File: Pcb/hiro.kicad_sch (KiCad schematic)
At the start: 0 parts

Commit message: schematic parts
added a really nice microsd card slot, an esp32-s3, and an audio jack.
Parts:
- added J1: Micro_SD_Card_Det_Hirose_DM3AT, symbol Connector:Micro_SD_Card_Det_Hirose_DM3AT
- added J2: AudioJack3, Connector_Audio:Jack_3.5mm_CUI_SJ-3523-SMT_Horizontal, symbol Connector_Audio:AudioJack3
- added U1: XIAO-ESP32-S3-Plus-SMD, Seeed_Studio_XIAO_Series:XIAO-ESP32-S3-Plus-SMD, symbol Seeed_Studio_XIAO_Series:XIAO-ESP32-S3 Plus-SMD
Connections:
- new net +3.3V: J1.4 (VDD)
- new net CLK: J1.5 (CLK), U1.23 (GPIO13_DVP_PCLK_SPI_SCK1)
- new net CMD: J1.3 (CMD), U1.21 (GPIO11_DVP_Y8_SPI_MOSI1)
- new net DAT0: J1.7 (DAT0), U1.22 (GPIO12_DVP_Y7_SPI_MISO1)
- new net DAT3: J1.2 (DAT3/CD)
- new net GND: J1.6 (VSS)
- no-connect marks 0 -> 2

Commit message: sooooooooooooooo much work
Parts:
- added C1, C4, C5, C6: 10 µF, Capacitor_SMD:C_01005_0402Metric_Pad0.57x0.30mm_HandSolder, symbol Device:C
- added C2, C3: 100nF, Capacitor_SMD:C_01005_0402Metric_Pad0.57x0.30mm_HandSolder, symbol Device:C
- added J3: Conn_01x08, symbol Connector_Generic:Conn_01x08
- added SW1, SW2: SW_Push, symbol Switch:SW_Push
- added U2: PCM5102A, Package_SO:TSSOP-20_4.4x6.5mm_P0.65mm, symbol Audio:PCM5102A
- J1: footprint (none) -> Connector_Card:microSD_HC_Hirose_DM3AT-SF-PEJM5
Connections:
- net +3.3V: now also U1.12 (3V3), C4.1, J3.1 (Pin_1), U2.17 (XSMT); no longer J1.4 (VDD)
- net CLK: now also U1.9 (GPIO7_A8_D8_SCK), J3.4 (Pin_4); no longer J1.5 (CLK), U1.23 (GPIO13_DVP_PCLK_SPI_SCK1)
- net GND: now also J2.S, U1.13 (GND), C2.1, C3.1, C4.2, C5.2, C6.2, J3.2 (Pin_2), U2.1 (CPVDD), U2.10 (DEMP), U2.11 (FLT), U2.16 (FMT), U2.19 (DGND), U2.3 (CPGND), U2.9 (AGND); no longer J1.6 (VSS)
- net at J2.R: now also U2.7 (OUTR)
- net at J2.T: now also U2.6 (OUTL)
- net CS: now reaches U1.10 (GPIO8_A9_D9_MISO)
- net CS: now also J3.5 (Pin_5)
- net DIN: now reaches U1.11 (GPIO9_A10_D10_MOSI)
- net DIN: now also J3.3 (Pin_3)
- net DC: now reaches U1.8 (GPIO44_D7_RX)
- net DC: now also J3.6 (Pin_6)
- net CMD: no longer names the net of J1.3 (CMD)
- net CMD: no longer U1.21 (GPIO11_DVP_Y8_SPI_MOSI1)
- net DAT0: no longer names the net of J1.7 (DAT0)
- net DAT0: no longer U1.22 (GPIO12_DVP_Y7_SPI_MISO1)
- net DAT3: no longer names the net of J1.2 (DAT3/CD)
- new net: C5.1, U2.18 (LDOO)
- new net: C1.1, U2.2 (CAPP)
- new net: C3.2, U2.20 (DVDD)
- new net: C1.2, U2.4 (CAPM)
- new net: C6.1, U2.5 (VNEG)
- new net: C2.2, U2.8 (AVDD)
- new net BCK: U2.13 (BCK)
- new net BL: J3.8 (Pin_8), U1.22 (GPIO12_DVP_Y7_SPI_MISO1)
- new net DIN2: U2.14 (DIN)
- new net LCK: U2.15 (LRCK)
- new net RST: J3.7 (Pin_7), U1.21 (GPIO11_DVP_Y8_SPI_MOSI1)
- no-connect marks 2 -> 1
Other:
- moved on the sheet: J2

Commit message: THE OUTLINE WORKS YAYYY
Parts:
- C1, C2, C3, C4, C5, C6: footprint Capacitor_SMD:C_01005_0402Metric_Pad0.57x0.30mm_HandSolder -> Capacitor_SMD:C_0603_1608Metric_Pad1.08x0.95mm_HandSolder
- J3: footprint (none) -> Connector_PinHeader_2.54mm:PinHeader_1x08_P2.54mm_Vertical
- U1: footprint Seeed_Studio_XIAO_Series:XIAO-ESP32-S3-Plus-SMD -> New_XIAO_Series_Footprints:XIAO-ESP32-S3-Plus-SMD
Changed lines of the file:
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@@
 			)
 		)
-		(property "Footprint" "Capacitor_SMD:C_01005_0402Metric_Pad0.57x0.30mm_HandSolder"
+		(property "Footprint" "Capacitor_SMD:C_0603_1608Metric_Pad1.08x0.95mm_HandSolder"
 			(at 159.7152 59.69 0)
 			(hide yes)
@@
 			)
 		)
-		(property "Footprint" "Capacitor_SMD:C_01005_0402Metric_Pad0.57x0.30mm_HandSolder"
+		(property "Footprint" "Capacitor_SMD:C_0603_1608Metric_Pad1.08x0.95mm_HandSolder"
 			(at 179.07 86.6648 0)
 			(hide yes)
@@
 			)
 		)
-		(property "Footprint" "Capacitor_SMD:C_01005_0402Metric_Pad0.57x0.30mm_HandSolder"
+		(property "Footprint" "Capacitor_SMD:C_0603_1608Metric_Pad1.08x0.95mm_HandSolder"
 			(at 162.2552 59.69 0)
 			(hide yes)
@@
 			)
 		)
-		(property "Footprint" "Capacitor_SMD:C_01005_0402Metric_Pad0.57x0.30mm_HandSolder"
+		(property "Footprint" "Capacitor_SMD:C_0603_1608Metric_Pad1.08x0.95mm_HandSolder"
 			(at 135.5852 46.99 0)
 			(hide yes)
@@
 			)
 		)
-		(property "Footprint" "Capacitor_SMD:C_01005_0402Metric_Pad0.57x0.30mm_HandSolder"
+		(property "Footprint" "Capacitor_SMD:C_0603_1608Metric_Pad1.08x0.95mm_HandSolder"
 			(at 172.4152 80.01 0)
 			(hide yes)
@@
 			)
 		)
-		(property "Footprint" "Capacitor_SMD:C_01005_0402Metric_Pad0.57x0.30mm_HandSolder"
+		(property "Footprint" "Capacitor_SMD:C_0603_1608Metric_Pad1.08x0.95mm_HandSolder"
 			(at 179.07 84.1248 0)
 			(hide yes)
@@
 			)
 		)
-		(property "Footprint" "Seeed_Studio_XIAO_Series:XIAO-ESP32-S3-Plus-SMD"
+		(property "Footprint" "New_XIAO_Series_Footprints:XIAO-ESP32-S3-Plus-SMD"
 			(at 74.422 37.846 0)
 			(hide yes)
@@
 			)
 		)
-		(property "Footprint" ""
+		(property "Footprint" "Connector_PinHeader_2.54mm:PinHeader_1x08_P2.54mm_Vertical"
 			(at 121.92 69.85 0)
 			(hide yes)

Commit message: Some stuff
it is def broken rn will fix laterrr
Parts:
- removed SW1, SW2: SW_Push, symbol Switch:SW_Push
- added S1, S2, S3: B3U-3100P-B, Button_Switch_SMD:SW_SPST_B3U-3100P, symbol B3U-3100P-B:B3U-3100P-B
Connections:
- net +3.3V: now also J1.4 (VDD)
- net BCK: now also U1.16 (GPIO39_CAM_SCL_I2S_SCK)
- net CLK: now also J1.5 (CLK), U1.3 (GPIO3_A2_D2)
- net DIN2: now also U1.15 (GPIO38_DVP_VSYNC_I2S_SD)
- net GND: now also J1.6 (VSS), J1.SH (SHIELD), U1.27 (GND1), S1.1, S1.3, S2.1, S2.3, S3.1, S3.3
- net LCK: now also U1.17 (GPIO40_CAM_SDA_I2S_WS)
- net SD_CS: now reaches U1.1 (GPIO1_A0_D0)
- net CMD: now reaches U1.2 (GPIO2_A1_D1)
- net SW3: now reaches U1.25 (GPIO40_MTDO_CAM_SDA_I2S_WS)
- net SW3: now also S3.2
- net SW2: now reaches U1.28 (GPIO42_MTMS_PDM_CLK_TX1)
- net SW2: now also S2.2
- net SW1: now reaches U1.29 (GPIO39_MTCK_CAM_SCL_I2S_SCK)
- net SW1: now also S1.2
- net BL renamed MISO
- net DIN renamed DIN1
- net RST renamed MOSI
- no-connect marks 1 -> 7
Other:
- moved on the sheet: J1

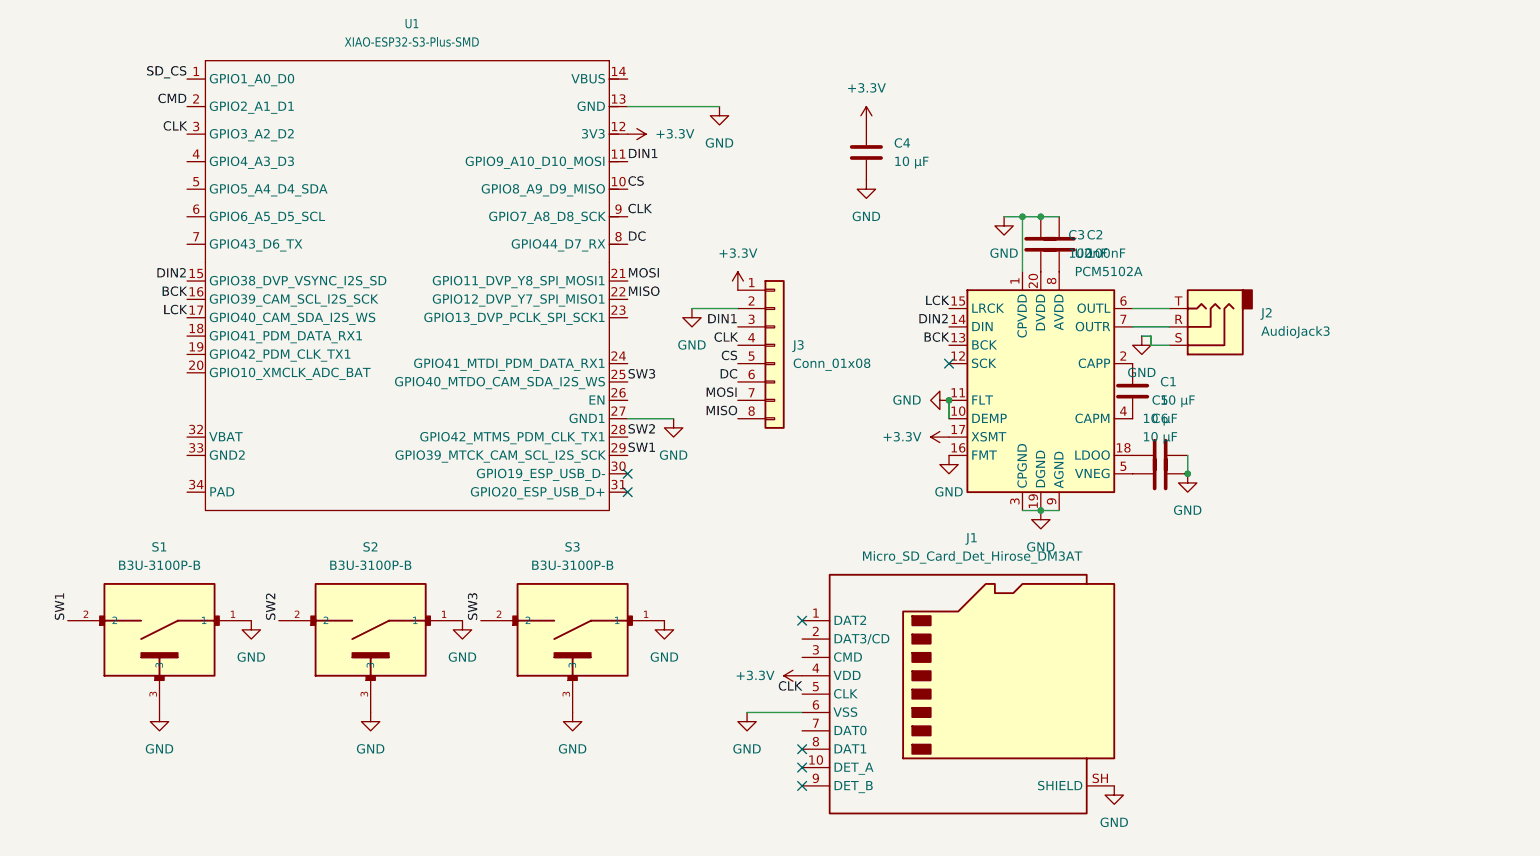
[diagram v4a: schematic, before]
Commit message: got a sideway switch working correctly.
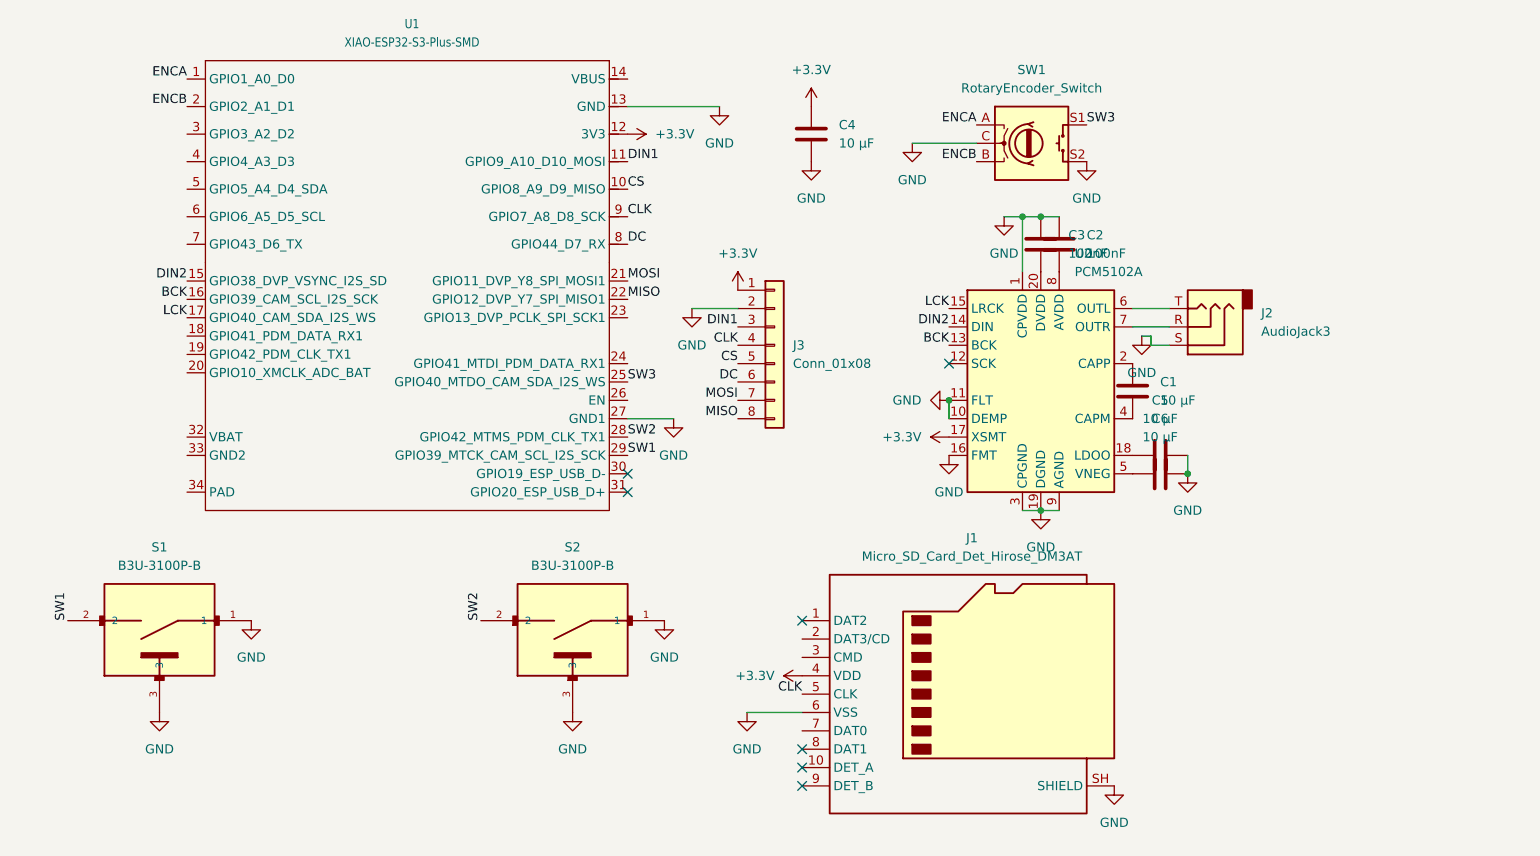
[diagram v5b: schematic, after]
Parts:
- removed S2: B3U-3100P-B, Button_Switch_SMD:SW_SPST_B3U-3100P, symbol B3U-3100P-B:B3U-3100P-B
- added SW1: RotaryEncoder_Switch, Libs:Right angle EC11 Rotary Encoder, symbol Device:RotaryEncoder_Switch
- renumbered S3 to S2
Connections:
- net CLK: no longer U1.3 (GPIO3_A2_D2)
- net GND: now also SW1.C, SW1.S2
- net SW2: now also S2.2
- net SW3: now also SW1.S1; no longer S2.2
- net CMD renamed ENCB
- net ENCB: now also SW1.B
- net SD_CS renamed ENCA
- net ENCA: now also SW1.A
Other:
- moved on the sheet: C4

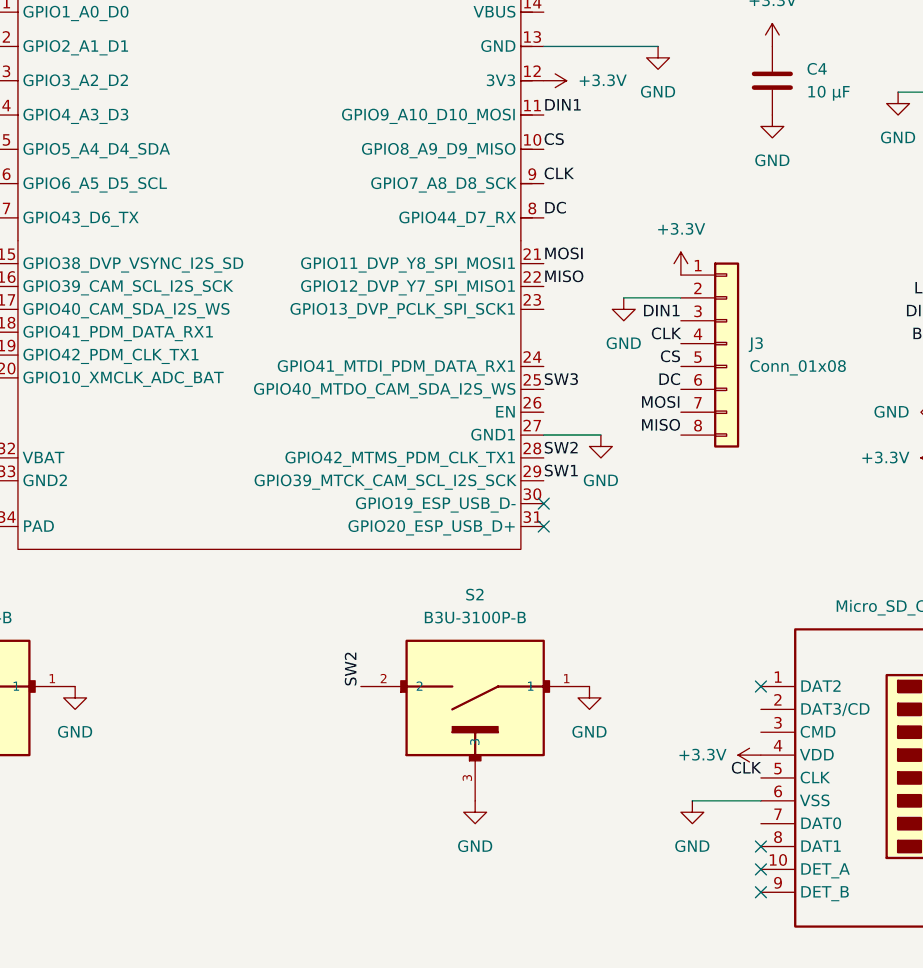
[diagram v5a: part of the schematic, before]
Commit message: Speaker + Speaker amp and 3d model
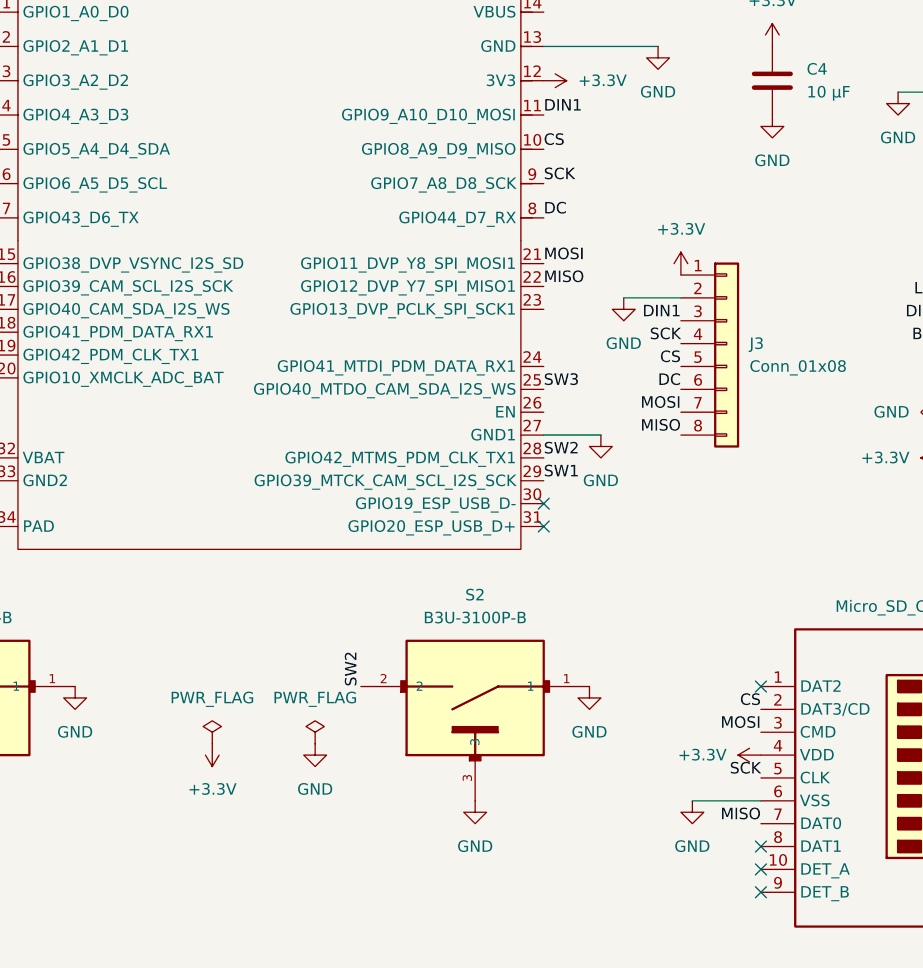
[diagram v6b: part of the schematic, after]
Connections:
- net CS: now also J1.2 (DAT3/CD)
- net MISO: now also J1.7 (DAT0)
- net MOSI: now also J1.3 (CMD)
- net CLK renamed SCK

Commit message: Some stuffs
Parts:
- added BT1: 4000mah, symbol Device:Battery
- added LS2: CVS-3108, Spkr:CUI_CVS-3108, symbol CVS-3108:CVS-3108
- added U3: MAX98357A, Package_DFN_QFN:TQFN-16-1EP_3x3mm_P0.5mm_EP1.23x1.23mm, symbol Audio:MAX98357A
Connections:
- net +3.3V: now also U3.7 (VDD), U3.8 (VDD)
- net BCK: now also U3.16 (BCLK)
- net CS: no longer J1.2 (DAT3/CD)
- net DIN1: now also U3.1 (DIN)
- net GND: now also U3.11 (GND), U3.15 (GND), U3.17 (PAD), U3.3 (GND)
- net LCK: now also U3.14 (LRCLK)
- net CS1: now reaches U1.23 (GPIO13_DVP_PCLK_SPI_SCK1)
- net CS1: now also J1.2 (DAT3/CD)
- net at U1.32 (VBAT): now also BT1.1 (+)
- net at U1.33 (GND2): now also BT1.2 (-)
- new net: LS2.N, U3.10 (OUTN)
- new net: LS2.P, U3.9 (OUTP)
- no-connect marks 7 -> 21

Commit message: New Speaker, some new cad, other stuff, renders, etc
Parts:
- removed BT1: 4000mah, symbol Device:Battery
- removed LS2: CVS-3108, Spkr:CUI_CVS-3108, symbol CVS-3108:CVS-3108
- added J4: Conn_01x02, Connector_JST:JST_PH_S2B-PH-K_1x02_P2.00mm_Horizontal, symbol Connector_Generic:Conn_01x02
- added LS1: CVS-1708, Spkr:SPKR_CVS-1708, symbol CVS-1708:CVS-1708
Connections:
- net at U3.10 (OUTN): now also LS1.M
- net at U3.9 (OUTP): now also LS1.P
- net at U1.32 (VBAT): now also J4.2 (Pin_2)
- net at U1.33 (GND2): now also J4.1 (Pin_1)
